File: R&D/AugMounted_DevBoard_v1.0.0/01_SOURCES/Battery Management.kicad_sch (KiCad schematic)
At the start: 2 parts, among them U2 U_BQ24296MRGER, U3 U_MAX17048G+T10

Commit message: Schematic 90% done
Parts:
- added C18, C19: C_0805_2.2uF_25V_X7R_20%, .mounted-lib:C_0805_1608Metric, symbol .mounted-lib:C_0805_2.2uF_25V_X7R_20%
- added C20, C21, C22, C23: C_1206_10uF_25V_X7R_10%, .mounted-lib:C_1206_3216Metric, symbol .mounted-lib:C_1206_10uF_25V_X7R_10%
- added C24, C25: C_0805_1uF_100V_X7S_20%, .mounted-lib:C_0805_1608Metric, symbol .mounted-lib:C_0805_1uF_100V_X7S_20%
- added C26, C33, C43: C_0603_100nF_100V_X7R_10%, .mounted-lib:C_0603_1608Metric, symbol .mounted-lib:C_0603_100nF_100V_X7R_10%
- added C27: C_0603_1.2nF_100V_X7R_5%, .mounted-lib:C_0603_1608Metric, symbol .mounted-lib:C_0603_1.2nF_100V_X7R_5%
- added C28, C31, C32, C36, C37, C40, C41: C_0805_10uF_10V_X7R_10%, .mounted-lib:C_0805_1608Metric, symbol .mounted-lib:C_0805_10uF_10V_X7R_10%
- added C38: C_0603_47nF_100V_X7R_10%, .mounted-lib:C_0603_1608Metric, symbol .mounted-lib:C_0603_47nF_100V_X7R_10%_1
- added C39: C_0603_4.7uF_16V_X7R_10%, .mounted-lib:C_0603_1608Metric, symbol .mounted-lib:C_0603_4.7uF_16V_X7R_10%
- added C42: C_0603_1uF_16V_X7R_10%, .mounted-lib:C_0603_1608Metric, symbol .mounted-lib:C_0603_1uF_16V_X7R_10%_1
- added D2: D_V2FM10HM3/H, .mounted-lib:D_SMF_VISHAY, symbol .mounted-lib:D_V2FM10HM3/H
- added D4: D_1SS301, .mounted-lib:SOT-23_TOSHIBA, symbol .mounted-lib:D_1SS301
- added D5: D_SRV05-4, .mounted-lib:SOT-23-6_TECH_PUBLIC, symbol .mounted-lib:D_SRV05-4
- added J3: J_JST_S2B-PH-SM4-TB, .mounted-lib:J_JST_S2B-PH-SM4-TB, symbol .mounted-lib:J_JST_S2B-PH-SM4-TB
- added L1: L_7447789003, .mounted-lib:L_7447789003, symbol .mounted-lib:L_7447789003
- added L3: L_TFM252012ALMA1R0MTAA, .mounted-lib:TFM252012ALMA1R0MTAA, symbol .mounted-lib:L_TFM252012ALMA1R0MTAA
- added L4: L_FNR3015S2R2MT, .mounted-lib:L_FNR3015S2R2MT, symbol .mounted-lib:L_FNR3015S2R2MT
- added Q2, Q4, Q5: Q_BSS123WQ-7-F, .mounted-lib:SOT-323_SC-70_DIODES_INC, symbol .mounted-lib:Q_BSS123WQ-7-F
- added Q3, Q6: Q_HSS2P10, .mounted-lib:SOT-23-3_HUASHUO, symbol .mounted-lib:Q_HSS2P10
- added R10, R20, R21, R7, R9: R_0603_100k_1%_0.1W, .mounted-lib:R_0603_1608Metric, symbol .mounted-lib:R_0603_100k_1%_0.1W
- added R11, R13, R8: R_0603_1M_1%_0.1W, .mounted-lib:R_0603_1608Metric, symbol .mounted-lib:R_0603_1M_1%_0.1W
- added R12, R22: R_0603_0R_1%_0.1W, .mounted-lib:R_0603_1608Metric, symbol .mounted-lib:R_0603_0R_1%_0.1W
- added R14, R17, R18: R_0603_10k_1%_0.1W, .mounted-lib:R_0603_1608Metric, symbol .mounted-lib:R_0603_10k_1%_0.1W
- added R15: R_0603_31.2k_0.5%_0.1W, .mounted-lib:R_0603_1608Metric, symbol .mounted-lib:R_0603_31.2k_0.5%_0.1W
- added R16: R_0603_5.23k_1%_0.1W, .mounted-lib:R_0603_1608Metric, symbol .mounted-lib:R_0603_5.23k_1%_0.1W
- added R19: R_0603_316R_0.5%_0.1W, .mounted-lib:R_0603_1608Metric, symbol .mounted-lib:R_0603_316R_0.5%_0.1W
- added R4: R_0603_42.2k_1%_0.1W, .mounted-lib:R_0603_1608Metric, symbol .mounted-lib:R_0603_42.2k_1%_0.1W
- added R5: R_0603_200k_1%_0.1W, .mounted-lib:R_0603_1608Metric, symbol .mounted-lib:R_0603_200k_1%_0.1W
- added R6: R_0603_26.7k_1%_0.1W, .mounted-lib:R_0603_1608Metric, symbol .mounted-lib:R_0603_26.7k_1%_0.1W
- added RT1: RT_TX06F103F3435ER, .mounted-lib:NTCG16_XXX_TDK, symbol .mounted-lib:RT_TX06F103F3435ER
- added SJ1: SOLDER_JUMPER_3PIN_NC, .mounted-lib:SOLDER_JUMPER_3PIN_NC, symbol .mounted-lib:SOLDER_JUMPER_3PIN_NC
- added TP4: TESTPOINT_1.5MM, .mounted-lib:TESTPOINT_1.5MM, symbol .mounted-lib:TESTPOINT_1.5MM
- added U10: U_TPS63001DRCR, .mounted-lib:PVSON-N10_TEXAS_INSTRUMENTS, symbol .mounted-lib:U_TPS63001DRCR
- added U7: U_LP3987H-18B5F, .mounted-lib:SOT-23-5_LOW_POWER, symbol .mounted-lib:U_LP3987H-18B5F
- added U8: U_TPS61087DRCR, .mounted-lib:PVSON-N10_TEXAS_INSTRUMENTS, symbol .mounted-lib:U_TPS61087DRCR
- U2: footprint (none) -> .mounted-lib:VQFN-24_TEXAS_INSTRUMENTS
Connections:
- net GND: now reaches U3.1 (CTG)
- net GND: now also U2.17 (PGND), U2.18 (PGND), U2.2 (PSEL), U2.9 (~{CE}), U3.4 (GND), U3.6 (QSTRT), U3.9 (PAD), C18.2, C19.2, C20.2, C21.2, C22.2, C23.2, C24.2, C25.2, C26.2, C27.2, C28.2, C31.2, C32.2, C33.2, C36.2, C37.2, C39.2, C40.2, C41.2, C42.2, C43.2, D5.2 (VN), J3.1 (-), J3.3, J3.4, Q2.2 (S), Q4.2 (S), Q5.2 (S), R11.2, R13.2, R15.2, R19.1, R21.2, R6.2, R8.2, RT1.2, SJ1.1 (A), U10.11 (EPAD), U10.3 (PGND), U10.9 (GND), U7.2 (GND), U8.11 (PAD), U8.4 (AGND), U8.5 (PGND)
- net VSYS_UNCUT: now reaches U3.2 (CELL+)
- net VSYS_UNCUT: now also U3.3 (VDD), C36.1, C37.1, C43.1, L3.2, Q3.2 (S), R10.1, R9.1, SJ1.3 (B)
- net at U3.5 (~{ALRT}): now also TP4.1
- net SCL: now reaches U3.7 (SCL)
- net SCL: now also U2.5 (SCL)
- net SDA: now reaches U3.8 (SDA)
- net SDA: now also U2.6 (SDA)
- net VBUS: now reaches U2.1 (VBUS), U2.24 (VBUS)
- net VBUS: now also C42.1
- net at U2.10 (ILIM): now also R19.2
- net at U2.11 (TS): now also R16.1
- net VBAT: now reaches U2.13 (BAT), U2.14 (BAT)
- net VBAT: now also C40.1, D5.5 (VP), J3.2 (+)
- net VSYS: now reaches U2.15 (SYS), U2.16 (SYS)
- net VSYS: now also C24.1, C25.1, C32.1, C33.1, L1.1, Q3.3 (D), U10.5 (VIN), U10.6 (EN), U10.7 (PS/SYNC), U10.8 (VINA), U8.8 (IN), U8.9 (FREQ)
- net at U2.19 (SW), U2.20 (SW): now also C38.1, L3.1
- net at U2.21 (BTST): now also C38.2
- net at U2.22 (REGN): now also C39.1
- net at U2.23 (PMID): now also C41.1
- net at U2.3 (~{PG}): now also R17.2
- net at U2.4 (STAT): now also R18.1
- net at U2.7 (INT): now also R14.2
- net at U2.8 (OTG): now also SJ1.2 (C)
- new net: D2.2 (A), L1.2, U8.6 (SW), U8.7 (SW)
- new net: C27.1, R4.2
- new net: Q3.1 (G), R10.2, R12.1
- new net: D4.3 (K), Q2.1 (G), R13.1
- new net: Q2.3 (D), R12.2
- new net: R5.2, R6.1, U8.2 (FB)
- new net: R15.1, R16.2, RT1.1
- new net: R4.1, U8.1 (COMP)
- new net: Q6.1 (G), R20.2, R22.1
- new net: Q4.3 (D), R22.2
- new net: C26.1, U8.10 (SS)
- new net: L4.2, U10.2 (L2)
- new net: L4.1, U10.4 (L1)
- new net +10V: C20.1, C21.1, C22.1, C23.1, D2.1 (K), R5.1
- new net +1V8: C18.1, Q6.2 (S), R20.1, U7.5 (VOUT)
- new net +3.3V: C19.1, C28.1, C31.1, R14.1, R17.1, R18.2, R7.1, U10.1 (VOUT), U10.10 (FB), U7.1 (VIN), U7.3 (EN)
- new net 1.8V_ENABLE: Q4.1 (G), R11.1
- new net 1.8V_LCD: Q6.3 (D)
- new net 10V_ENABLE: R8.1, U8.3 (EN)
- new net ENCODER_S1: R9.2
- new net ENCODER_S2: D4.1 (A1), Q5.1 (G), R21.1
- new net ESP_ENCODER_BUTTON_PIN: Q5.3 (D), R7.2
- new net ESP_POWER_EN: D4.2 (A2)
- no-connect marks 0 -> 5
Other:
- moved on the sheet: U3

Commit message: Moved components
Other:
- moved on the sheet: C18, C19, C20, C21, C22, C23, C24, C25, C26, C27, C28, C31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

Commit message: Schematic done
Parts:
- added SJ2: SOLDER_JUMPER_3PIN_NC, .mounted-lib:SOLDER_JUMPER_3PIN_NC, symbol .mounted-lib:SOLDER_JUMPER_3PIN_NC
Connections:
- net GND: now also U2.25 (PAD), SJ2.1 (A); no longer U2.2 (PSEL)
- net VSYS_UNCUT: now also SJ2.3 (B)
- net PGOOD: now reaches R17.2, U2.3 (~{PG})
- net CHARGE_STATUS: now reaches R18.1, U2.4 (STAT)
- net ESP_ENCODER_BUTTON_PIN renamed ENCODER_BUTTON
- new net: SJ2.2 (C), U2.2 (PSEL)
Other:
- note added: "SET TO OFF BY DEFAULT"
- moved on the sheet: C18, C19, C20, C21, C22, C23, C24, C25, C26, C27, C28, C31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

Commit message: First revision of the layout
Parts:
- renumbered C42 to C302, C41 to C303, C43 to C305, C38 to C308, C40 to C309, C39 to C310, C36 to C312, C37 to C314, C33 to C?, C27 to C?, C23 to C?, C32 to C?, C20 to C?, C28 to C?, C18 to C?, C25 to C?, C19 to C?, C22 to C?, C21 to C?, C31 to C?, C26 to C?, C24 to C?, D5 to D301, D4 to D302, D2 to D?, J3 to J301, L4 to L301, L3 to L302, L1 to L?, Q4 to Q301, Q6 to Q302, Q5 to Q303, Q2 to Q304, Q3 to Q305, R19 to R301, R14 to R302, R17 to R303, R18 to R304, R11 to R305, R20 to R306, R22 to R307, R16 to R308, R15 to R309, R21 to R310, R7 to R311, R9 to R312, R13 to R313, R10 to R314, R12 to R315, R8 to R319, R5 to R?, R4 to R?, R6 to R?, RT1 to RT301, SJ1 to SJ301, SJ2 to SJ302, TP4 to TP301, U3 to U302, U2 to U303, U8 to U?, U7 to U?, U10 to U?

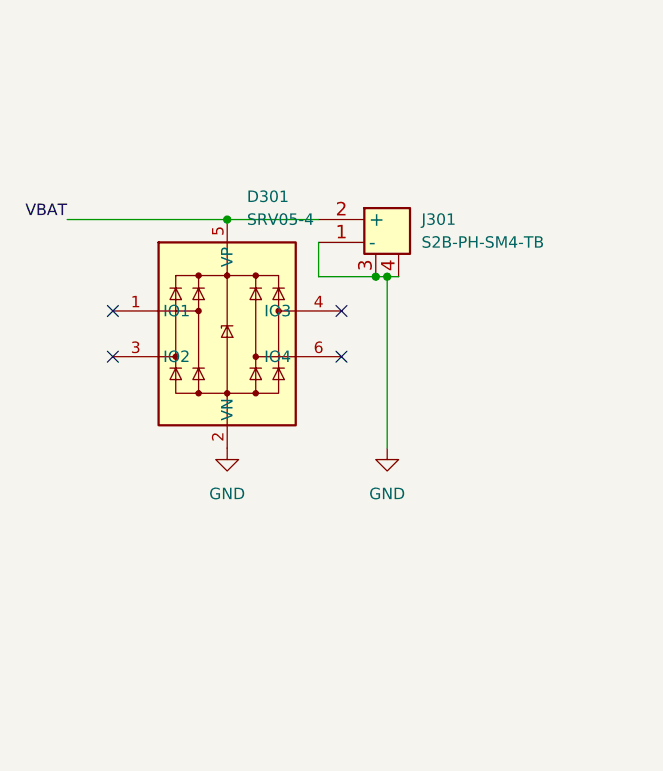
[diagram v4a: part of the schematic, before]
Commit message: Changed layout to a banana shape
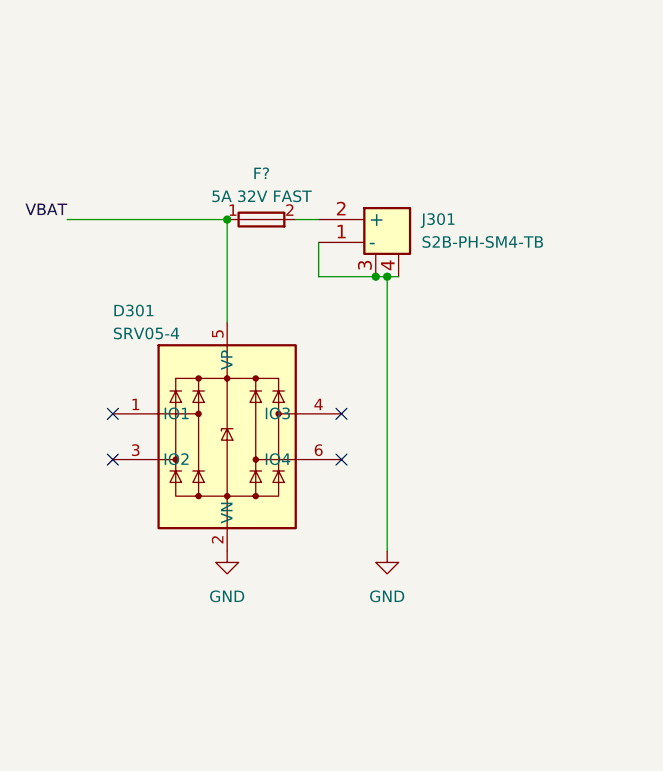
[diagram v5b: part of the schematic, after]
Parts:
- added F?: F_MFU0603FF05000P100, .mounted-lib:R_0603_1608Metric, symbol .mounted-lib:F_MFU0603FF05000P100
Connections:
- net VBAT: now also F?.1; no longer J301.2 (+)
- new net: F?.2, J301.2 (+)
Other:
- moved on the sheet: D301

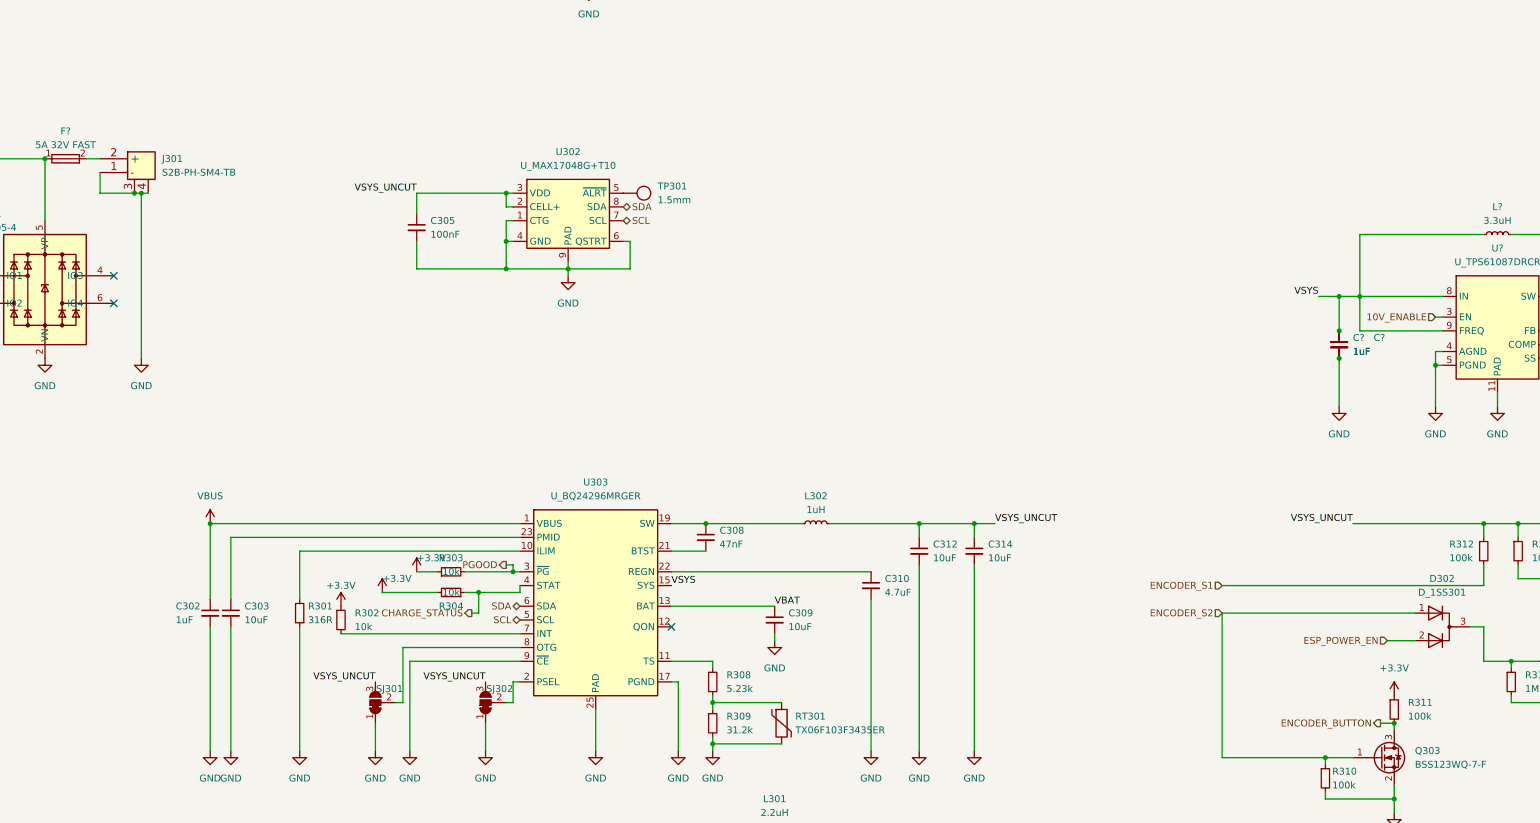
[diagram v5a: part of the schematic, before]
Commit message: Added resistors for CC1 and CC2 pins, layout is started on the high part of the board
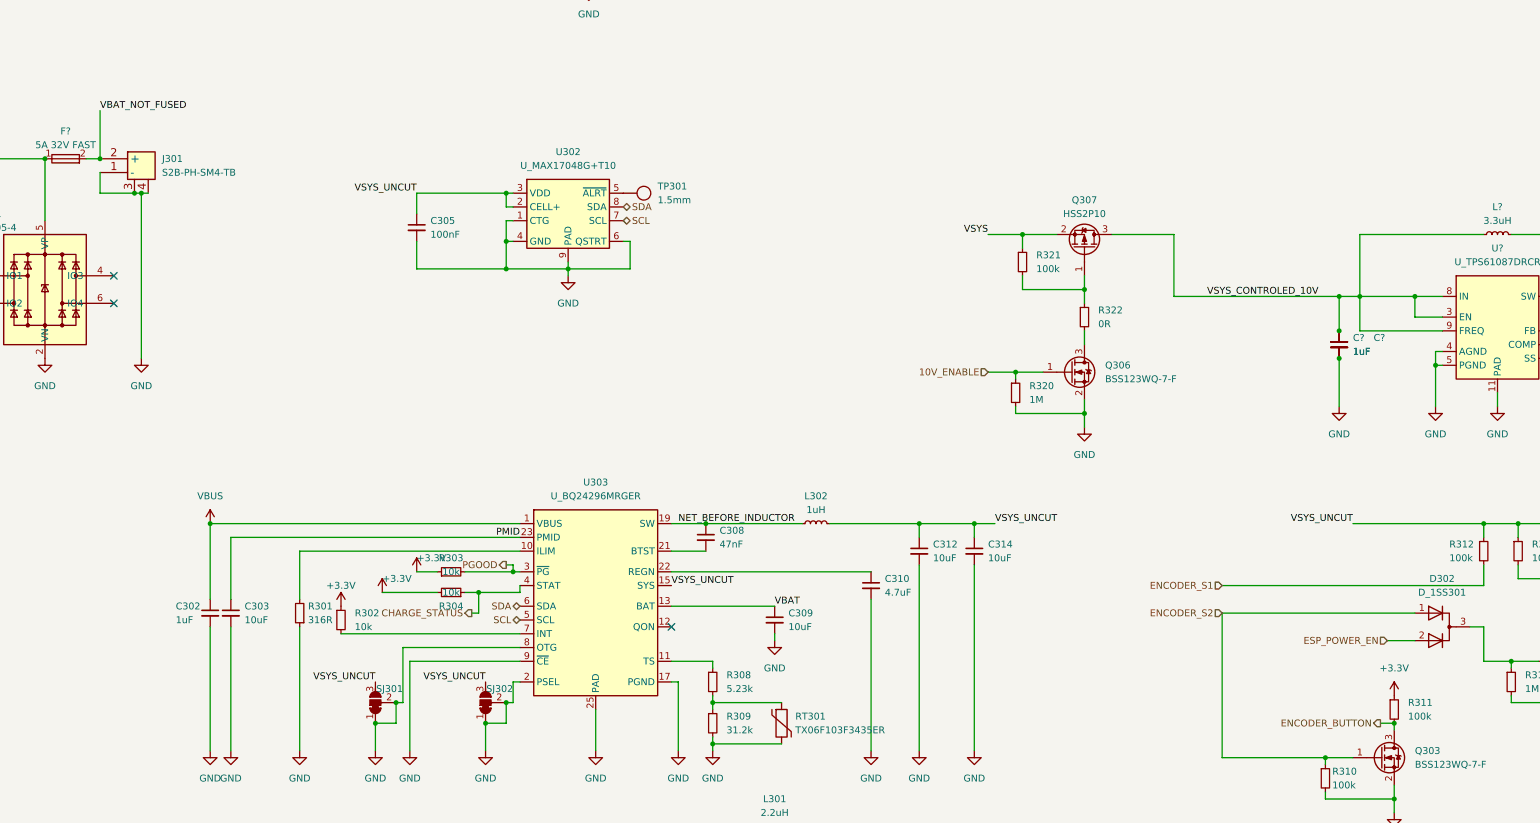
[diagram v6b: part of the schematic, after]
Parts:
- added Q306: Q_BSS123WQ-7-F, .mounted-lib:SOT-323_SC-70_DIODES_INC, symbol .mounted-lib:Q_BSS123WQ-7-F
- added Q307: Q_HSS2P10, .mounted-lib:SOT-23-3_HUASHUO, symbol .mounted-lib:Q_HSS2P10
- added R320: R_0603_1M_1%_0.1W, .mounted-lib:R_0603_1608Metric, symbol .mounted-lib:R_0603_1M_1%_0.1W
- added R321: R_0603_100k_1%_0.1W, .mounted-lib:R_0603_1608Metric, symbol .mounted-lib:R_0603_100k_1%_0.1W
- added R322: R_0603_0R_1%_0.1W, .mounted-lib:R_0603_1608Metric, symbol .mounted-lib:R_0603_0R_1%_0.1W
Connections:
- net 10V_ENABLE: now also Q306.1 (G), R320.1; no longer U?.3 (EN)
- net GND: now also SJ301.2 (C), SJ302.2 (C), U303.2 (PSEL), U303.8 (OTG), Q306.2 (S), R320.2
- net VSYS: now also Q307.2 (S), R321.1; no longer C?.1, C?.1, L?.1, U303.15 (SYS), U303.16 (SYS), U?.8 (IN), U?.9 (FREQ)
- net VSYS_UNCUT: now also U303.15 (SYS), U303.16 (SYS)
- net VBAT_NOT_FUSED: now reaches F?.2, J301.2 (+)
- net NET_BEFORE_INDUCTOR: now reaches C308.1, L302.1, U303.19 (SW), U303.20 (SW)
- net PMID: now reaches C303.1, U303.23 (PMID)
- new net: Q307.1 (G), R321.2, R322.1
- new net: Q306.3 (D), R322.2
- new net VSYS_CONTROLED_10V: C?.1, C?.1, L?.1, Q307.3 (D), U?.3 (EN), U?.8 (IN), U?.9 (FREQ)

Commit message: Changed layout + all passive to 0402
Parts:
- removed C308: C_0603_47nF_100V_X7R_10%, .mounted-lib:C_0603_1608Metric, symbol .mounted-lib:C_0603_47nF_100V_X7R_10%_1
- removed R301: R_0603_316R_0.5%_0.1W, .mounted-lib:R_0603_1608Metric, symbol .mounted-lib:R_0603_316R_0.5%_0.1W
- removed R302, R303, R304: R_0603_10k_1%_0.1W, .mounted-lib:R_0603_1608Metric, symbol .mounted-lib:R_0603_10k_1%_0.1W
- removed R308: R_0603_5.23k_1%_0.1W, .mounted-lib:R_0603_1608Metric, symbol .mounted-lib:R_0603_5.23k_1%_0.1W
- removed R319: R_0603_1M_1%_0.1W, .mounted-lib:R_0603_1608Metric, symbol .mounted-lib:R_0603_1M_1%_0.1W
- removed R?: R_0603_200k_1%_0.1W, .mounted-lib:R_0603_1608Metric, symbol .mounted-lib:R_0603_200k_1%_0.1W
- removed R?: R_0603_42.2k_1%_0.1W, .mounted-lib:R_0603_1608Metric, symbol .mounted-lib:R_0603_42.2k_1%_0.1W
- removed R?: R_0603_26.7k_1%_0.1W, .mounted-lib:R_0603_1608Metric, symbol .mounted-lib:R_0603_26.7k_1%_0.1W
- removed SJ301, SJ302: SOLDER_JUMPER_3PIN_NC, .mounted-lib:SOLDER_JUMPER_3PIN_NC, symbol .mounted-lib:SOLDER_JUMPER_3PIN_NC
- removed TP301: TESTPOINT_1.5MM, .mounted-lib:TESTPOINT_1.5MM, symbol .mounted-lib:TESTPOINT_1.5MM
- added C308: C_0402_47nF_50V_X7R_10%, .mounted-lib:C_0402_1005Metric, symbol .mounted-lib:C_0402_47nF_50V_X7R_10%
- added R301: R_0402_316R_1%_0.06W, .mounted-lib:R_0402_1005Metric, symbol .mounted-lib:R_0402_316R_1%_0.06W
- added R302, R303, R304: R_0402_10k_1%_0.06W, .mounted-lib:R_0402_1005Metric, symbol .mounted-lib:R_0402_10k_1%_0.06W
- added R308: R_0402_5.23k_1%_0.06W, .mounted-lib:R_0402_1005Metric, symbol .mounted-lib:R_0402_5.23k_1%_0.06W
- added R319: R_0402_42.2k_1%_0.06W, .mounted-lib:R_0402_1005Metric, symbol .mounted-lib:R_0402_42.2k_1%_0.06W
- added R320: R_0402_200k_1%_0.06W, .mounted-lib:R_0402_1005Metric, symbol .mounted-lib:R_0402_200k_1%_0.06W
- added R321: R_0402_26.7k_1%_0.06W, .mounted-lib:R_0402_1005Metric, symbol .mounted-lib:R_0402_26.7k_1%_0.06W
- added R323, R324: R_0402_0R_1%_0.06W, .mounted-lib:R_0402_1005Metric, symbol .mounted-lib:R_0402_0R_1%_0.06W
- C302: value C_0603_1uF_16V_X7R_10% -> C_0402_1uF_10V_X7R_10%; footprint .mounted-lib:C_0603_1608Metric -> .mounted-lib:C_0402_1005Metric; symbol .mounted-lib:C_0603_1uF_16V_X7R_10%_1 -> .mounted-lib:C_0402_1uF_10V_X7R_10%; MaxHeight_mm 0.8mm -> 0.5mm; Package C0603 -> C0402; Voltage 16V -> 10V
- C305, C?: footprint .mounted-lib:C_0603_1608Metric -> .mounted-lib:C_0402_1005Metric; symbol .mounted-lib:C_0603_100nF_100V_X7R_10% -> .mounted-lib:C_0402_100nF_50V_X7R_10%; MaxHeight_mm 0.8mm -> 0.5mm; Voltage 100V -> 50V
- C?: value C_0603_1.2nF_100V_X7R_5% -> C_0402_1.2nF_50V_X7R_10%; footprint .mounted-lib:C_0603_1608Metric -> .mounted-lib:C_0402_1005Metric; symbol .mounted-lib:C_0603_1.2nF_100V_X7R_5% -> .mounted-lib:C_0402_1.2nF_50V_X7R_10%; MaxHeight_mm 0.8mm -> 0.5mm; Package C0603 -> C0402; Tolerance 5% -> 10%; _Created TJO 2022-05-27 -> JCN 2023-11-24
- C? (x2): value C_0805_1uF_100V_X7S_20% -> C_0402_1uF_10V_X7R_10%; footprint .mounted-lib:C_0805_1608Metric -> .mounted-lib:C_0402_1005Metric; symbol .mounted-lib:C_0805_1uF_100V_X7S_20% -> .mounted-lib:C_0402_1uF_10V_X7R_10%; CMP_ID 7 -> 1069; MaxHeight_mm 1.25mm -> 0.5mm; Package C0805 -> C0402; Tolerance 20% -> 10%; Voltage 100V -> 10V; _Created CCN 2022-05-12 -> JCN 2023-11-12
- C?: footprint .mounted-lib:C_0603_1608Metric -> .mounted-lib:C_0402_1005Metric; symbol .mounted-lib:C_0603_100nF_100V_X7R_10% -> .mounted-lib:C_0402_100nF_50V_X7R_10%; CMP_ID 11 -> 1062; MaxHeight_mm 0.8mm -> 0.5mm; Voltage 100V -> 50V
- R305: footprint .mounted-lib:R_0603_1608Metric -> .mounted-lib:R_0402_1005Metric; symbol .mounted-lib:R_0603_1M_1%_0.1W -> .mounted-lib:R_0402_1M_1%_0.06W; MaxHeight_mm 0.55 -> 0.35MM; Package R0603 -> R0402; Power_W 0.1W -> 0.06W
- R306: value R_0603_100k_1%_0.1W -> R_0402_100k_1%_0.06W; footprint .mounted-lib:R_0603_1608Metric -> .mounted-lib:R_0402_1005Metric; symbol .mounted-lib:R_0603_100k_1%_0.1W -> .mounted-lib:R_0402_100k_1%_0.06W; CMP_ID 50 -> 1068; MaxHeight_mm 0.55mm -> 0.35mm; Package R0603 -> R0402; Power_W 0.1W -> 0.06W; _Created GCE 2022-05-12 -> JCN 2023-11-24
- R307: value R_0603_0R_1%_0.1W -> R_0402_0R_1%_0.06W; footprint .mounted-lib:R_0603_1608Metric -> .mounted-lib:R_0402_1005Metric; symbol .mounted-lib:R_0603_0R_1%_0.1W -> .mounted-lib:R_0402_0R_1%_0.06W; MaxHeight_mm 0.55 -> 0.35MM; Package R0603 -> R0402; Power_W 0.1W -> 0.06W
- R310: renamed from R320; footprint .mounted-lib:R_0603_1608Metric -> .mounted-lib:R_0402_1005Metric; symbol .mounted-lib:R_0603_1M_1%_0.1W -> .mounted-lib:R_0402_1M_1%_0.06W; MaxHeight_mm 0.55 -> 0.35MM; Package R0603 -> R0402; Power_W 0.1W -> 0.06W
- R311: renamed from R321; value R_0603_100k_1%_0.1W -> R_0402_100k_1%_0.06W; footprint .mounted-lib:R_0603_1608Metric -> .mounted-lib:R_0402_1005Metric; symbol .mounted-lib:R_0603_100k_1%_0.1W -> .mounted-lib:R_0402_100k_1%_0.06W; CMP_ID 50 -> 1068; MaxHeight_mm 0.55mm -> 0.35mm; Package R0603 -> R0402; Power_W 0.1W -> 0.06W; _Created GCE 2022-05-12 -> JCN 2023-11-24
- R312: renamed from R322; value R_0603_0R_1%_0.1W -> R_0402_0R_1%_0.06W; footprint .mounted-lib:R_0603_1608Metric -> .mounted-lib:R_0402_1005Metric; symbol .mounted-lib:R_0603_0R_1%_0.1W -> .mounted-lib:R_0402_0R_1%_0.06W; MaxHeight_mm 0.55 -> 0.35MM; Package R0603 -> R0402; Power_W 0.1W -> 0.06W
- R313: renamed from R310; value R_0603_100k_1%_0.1W -> R_0402_100k_1%_0.06W; footprint .mounted-lib:R_0603_1608Metric -> .mounted-lib:R_0402_1005Metric; symbol .mounted-lib:R_0603_100k_1%_0.1W -> .mounted-lib:R_0402_100k_1%_0.06W; CMP_ID 50 -> 1068; MaxHeight_mm 0.55mm -> 0.35mm; Package R0603 -> R0402; Power_W 0.1W -> 0.06W; _Created GCE 2022-05-12 -> JCN 2023-11-24
- R314: renamed from R311; value R_0603_100k_1%_0.1W -> R_0402_100k_1%_0.06W; footprint .mounted-lib:R_0603_1608Metric -> .mounted-lib:R_0402_1005Metric; symbol .mounted-lib:R_0603_100k_1%_0.1W -> .mounted-lib:R_0402_100k_1%_0.06W; CMP_ID 50 -> 1068; MaxHeight_mm 0.55mm -> 0.35mm; Package R0603 -> R0402; Power_W 0.1W -> 0.06W; _Created GCE 2022-05-12 -> JCN 2023-11-24
- R315: renamed from R312; value R_0603_100k_1%_0.1W -> R_0402_100k_1%_0.06W; footprint .mounted-lib:R_0603_1608Metric -> .mounted-lib:R_0402_1005Metric; symbol .mounted-lib:R_0603_100k_1%_0.1W -> .mounted-lib:R_0402_100k_1%_0.06W; CMP_ID 50 -> 1068; MaxHeight_mm 0.55mm -> 0.35mm; Package R0603 -> R0402; Power_W 0.1W -> 0.06W; _Created GCE 2022-05-12 -> JCN 2023-11-24
- R316: renamed from R313; footprint .mounted-lib:R_0603_1608Metric -> .mounted-lib:R_0402_1005Metric; symbol .mounted-lib:R_0603_1M_1%_0.1W -> .mounted-lib:R_0402_1M_1%_0.06W; MaxHeight_mm 0.55 -> 0.35MM; Package R0603 -> R0402; Power_W 0.1W -> 0.06W
- R317: renamed from R314; value R_0603_100k_1%_0.1W -> R_0402_100k_1%_0.06W; footprint .mounted-lib:R_0603_1608Metric -> .mounted-lib:R_0402_1005Metric; symbol .mounted-lib:R_0603_100k_1%_0.1W -> .mounted-lib:R_0402_100k_1%_0.06W; CMP_ID 50 -> 1068; MaxHeight_mm 0.55mm -> 0.35mm; Package R0603 -> R0402; Power_W 0.1W -> 0.06W; _Created GCE 2022-05-12 -> JCN 2023-11-24
- R318: renamed from R315; value R_0603_0R_1%_0.1W -> R_0402_0R_1%_0.06W; footprint .mounted-lib:R_0603_1608Metric -> .mounted-lib:R_0402_1005Metric; symbol .mounted-lib:R_0603_0R_1%_0.1W -> .mounted-lib:R_0402_0R_1%_0.06W; MaxHeight_mm 0.55 -> 0.35MM; Package R0603 -> R0402; Power_W 0.1W -> 0.06W
- renumbered Q306 to Q303, Q307 to Q304, Q303 to Q305, Q304 to Q306, Q305 to Q307
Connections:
- net +10V: now also R320.1
- net +3.3V: now also R302.1, R303.1, R304.1
- net CHARGE_STATUS: now also R304.2
- net GND: now also R301.2, R321.2, R323.2, R324.2; no longer U303.2 (PSEL), U303.8 (OTG)
- net NET_BEFORE_INDUCTOR: now also C308.1
- net PGOOD: now also R303.2
- net at U303.7 (INT): now also R302.2
- net at C?.1: now also R319.2
- net at U?.2 (FB): now also R320.2, R321.1
- net at R309.1, RT301.1: now also R308.2
- net at U?.1 (COMP): now also R319.1
- net at U303.11 (TS): now also R308.1
- net at U303.10 (ILIM): now also R301.1
- net at U303.21 (BTST): now also C308.2
- new net: R323.1, U303.8 (OTG)
- new net: R324.1, U303.2 (PSEL)
- no-connect marks 5 -> 6
